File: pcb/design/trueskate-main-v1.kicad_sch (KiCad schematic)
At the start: 0 parts

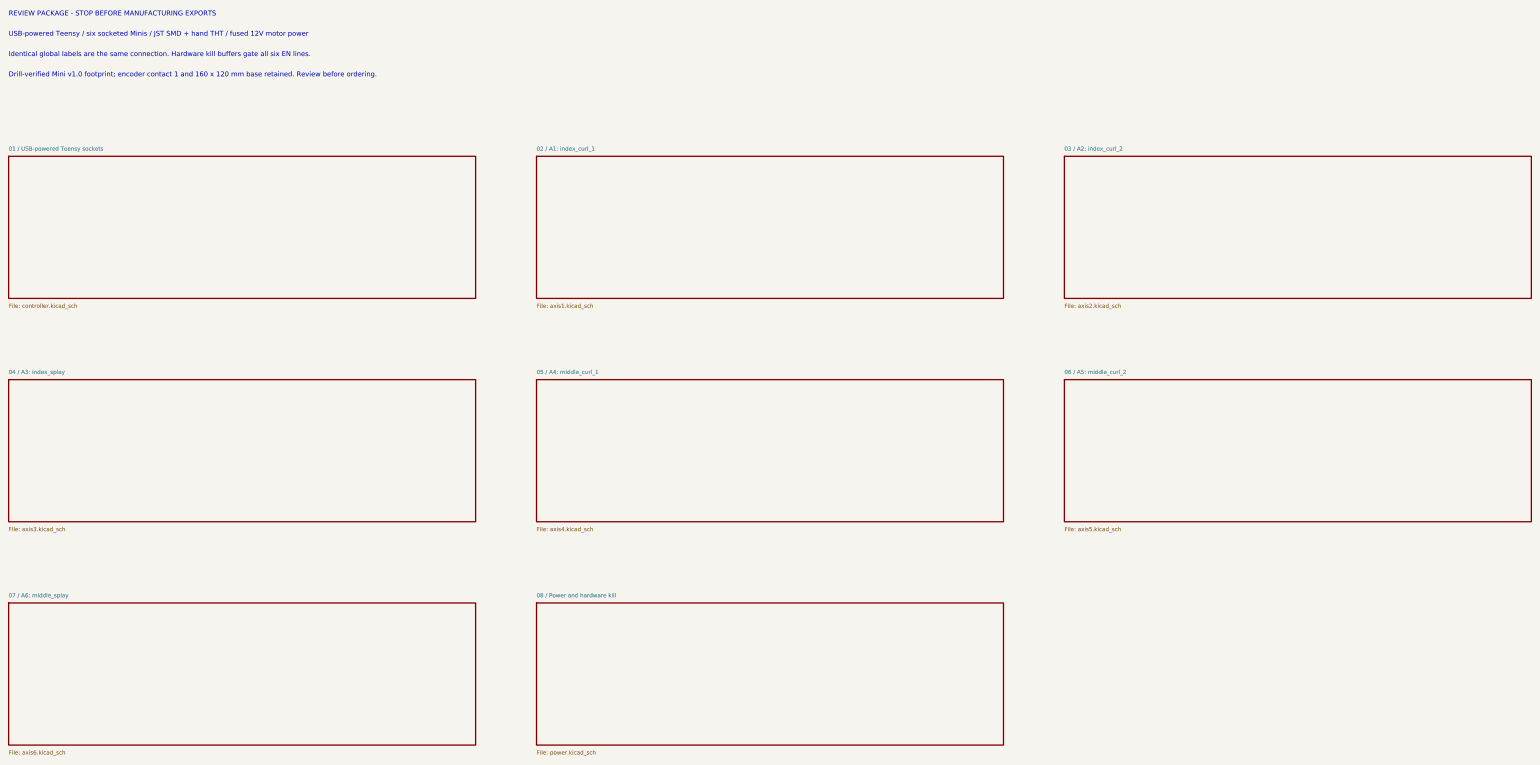
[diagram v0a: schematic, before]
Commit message: feat: finalize 3+3 carrier and bare PCB fabrication package
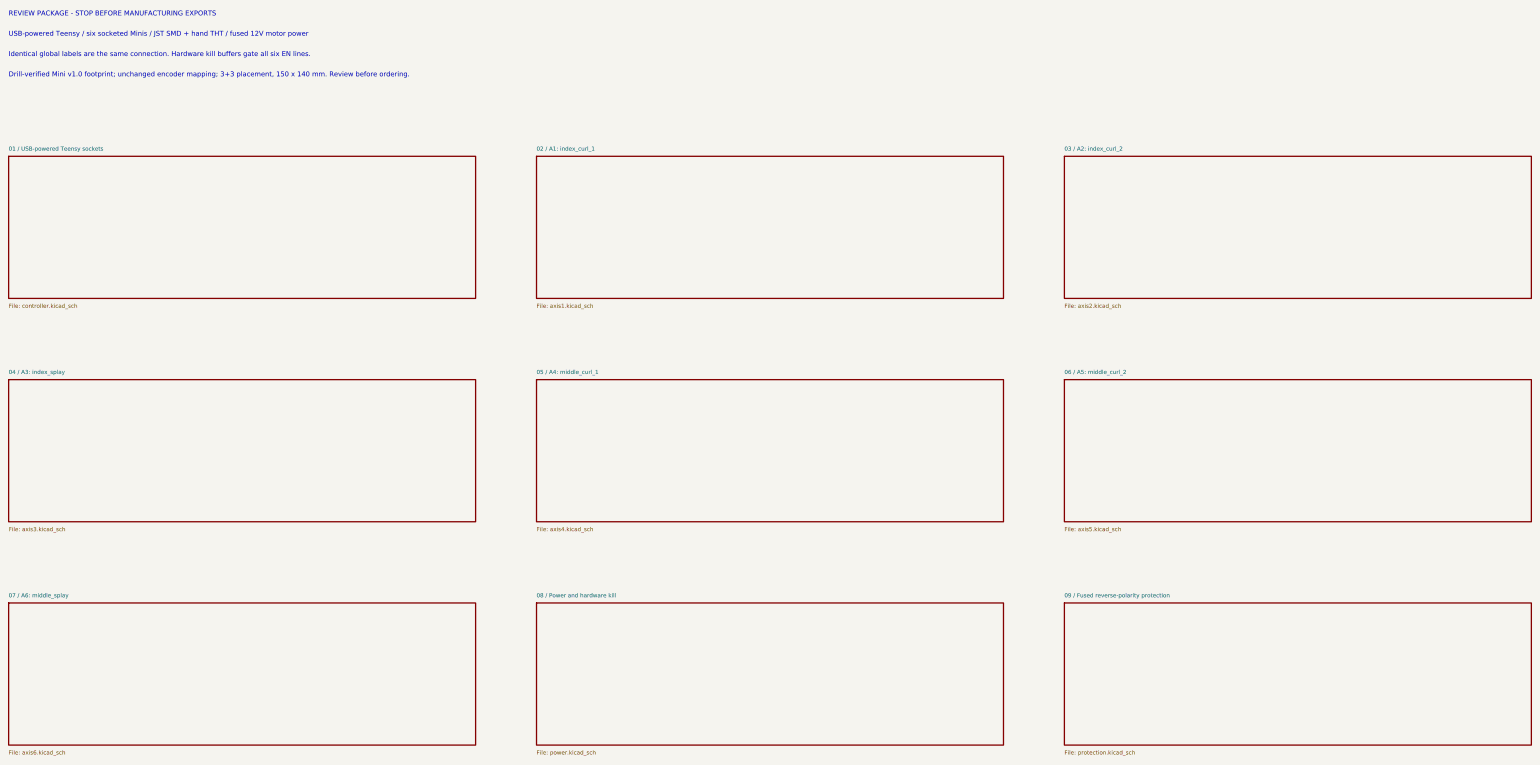
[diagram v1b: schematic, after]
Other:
- added sheet 09 / Fused reverse-polarity protection (protection.kicad_sch)
- note added: "Drill-verified Mini v1.0 footprint; unchanged encoder mapping; 3+3 placement, 150 x 140 mm. Review before ordering."
- note removed: "Drill-verified Mini v1.0 footprint; encoder contact 1 and 160 x 120 mm base retained. Review before ordering."
